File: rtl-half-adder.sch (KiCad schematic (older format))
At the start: 50 parts, among them Q1 Q_NPN_EBC, Q10 Q_NPN_EBC, Q11 Q_NPN_EBC, Q12 Q_NPN_EBC, Q13 Q_NPN_EBC, Q14 Q_NPN_EBC, Q15 Q_NPN_EBC, Q2 Q_NPN_EBC, Q3 Q_NPN_EBC, Q4 Q_NPN_EBC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

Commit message: add sheet annotations
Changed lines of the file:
@@
 encoding utf-8
 Sheet 1 2
-Title ""
-Date ""
-Rev ""
+Title "RTL Half Adder"
+Date "2019-06-12"
+Rev "v1"
 Comp ""
-Comment1 ""
-Comment2 ""
-Comment3 ""
-Comment4 ""
+Comment1 "creativecommons.org/licenses/by-nc-sa/4.0/"
+Comment2 "CC BY-NC-SA"
+Comment3 "github.com/tyehle/rtl-half-adder"
+Comment4 "Author: Tobin Yehle"
 $EndDescr
 Wire Wire Line
@@
 NoConn ~ 3450 1400
 NoConn ~ 3450 1950
+$Comp
+L Graphic:Logo_Open_Hardware_Large #LOGO?
+U 1 1 5D03E126
+P 6350 7200
+AR Path="/5D016A93/5D03E126" Ref="#LOGO?"  Part="1"
+AR Path="/5D03E126" Ref="#LOGO?"  Part="1"
+F 0 "#LOGO?" H 6350 7700 50  0001 C CNN
+F 1 "Logo_Open_Hardware_Large" H 6350 6800 50  0001 C CNN
+F 2 "" H 6350 7200 50  0001 C CNN
+F 3 "~" H 6350 7200 50  0001 C CNN
+	1    6350 7200
+	1    0    0    -1
+$EndComp
 $EndSCHEMATC

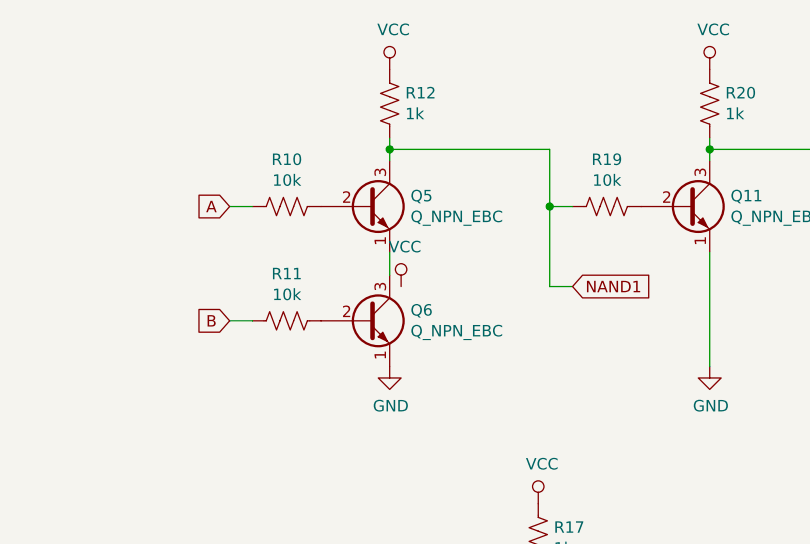
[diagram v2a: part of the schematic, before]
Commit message: more part links and BOM
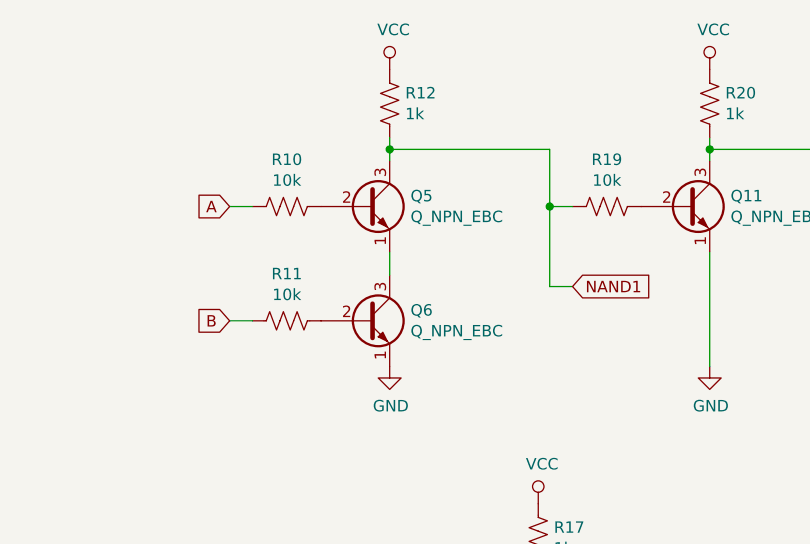
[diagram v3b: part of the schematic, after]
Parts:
- Q1, Q10, Q11, Q12, Q13, Q14, Q15, Q2, Q3, Q4, Q5, Q6, Q7, Q8, Q9: Link https://www.mouser.com/ProductDetail/PN2222A-T -> https://www.mouser.com/ProductDetail/2N3904BU
- R1, R10, R11, R13, R14, R15, R16, R19, R21, R22, R24, R25, R3, R5, R6, R7, R8: Link (none) -> https://www.mouser.com/ProductDetail/CFR-25JT-52-10K
- R12, R17, R18, R20, R23, R9: Link (none) -> https://www.mouser.com/ProductDetail/CFR-25JT-52-1K

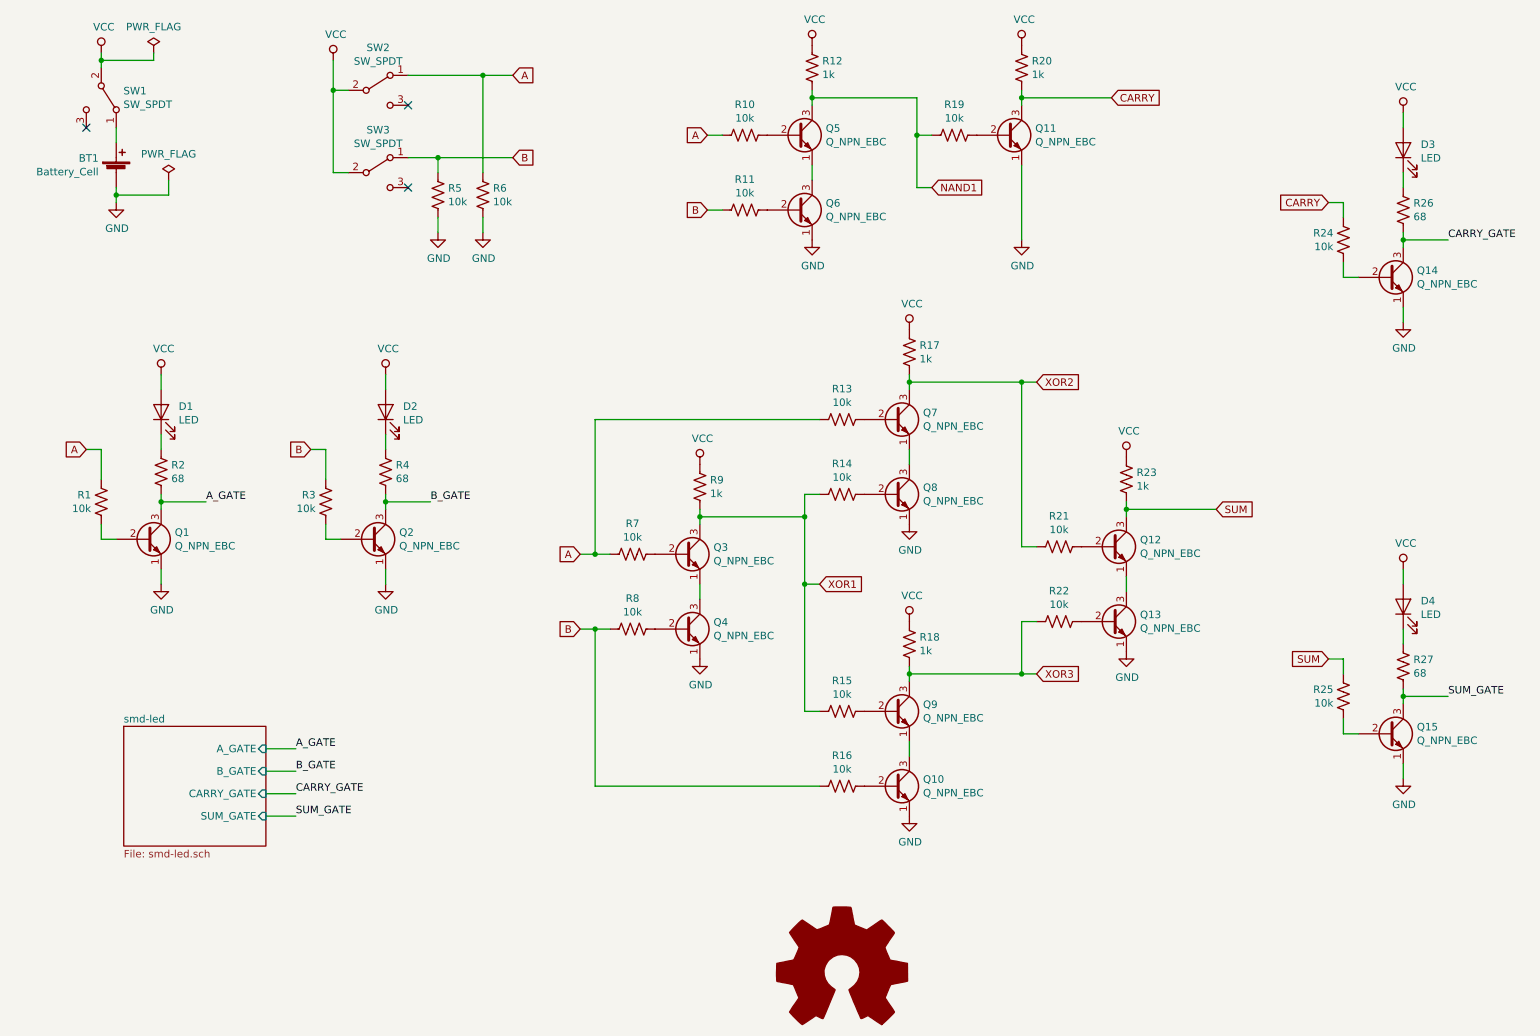
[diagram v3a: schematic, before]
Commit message: add io led specs
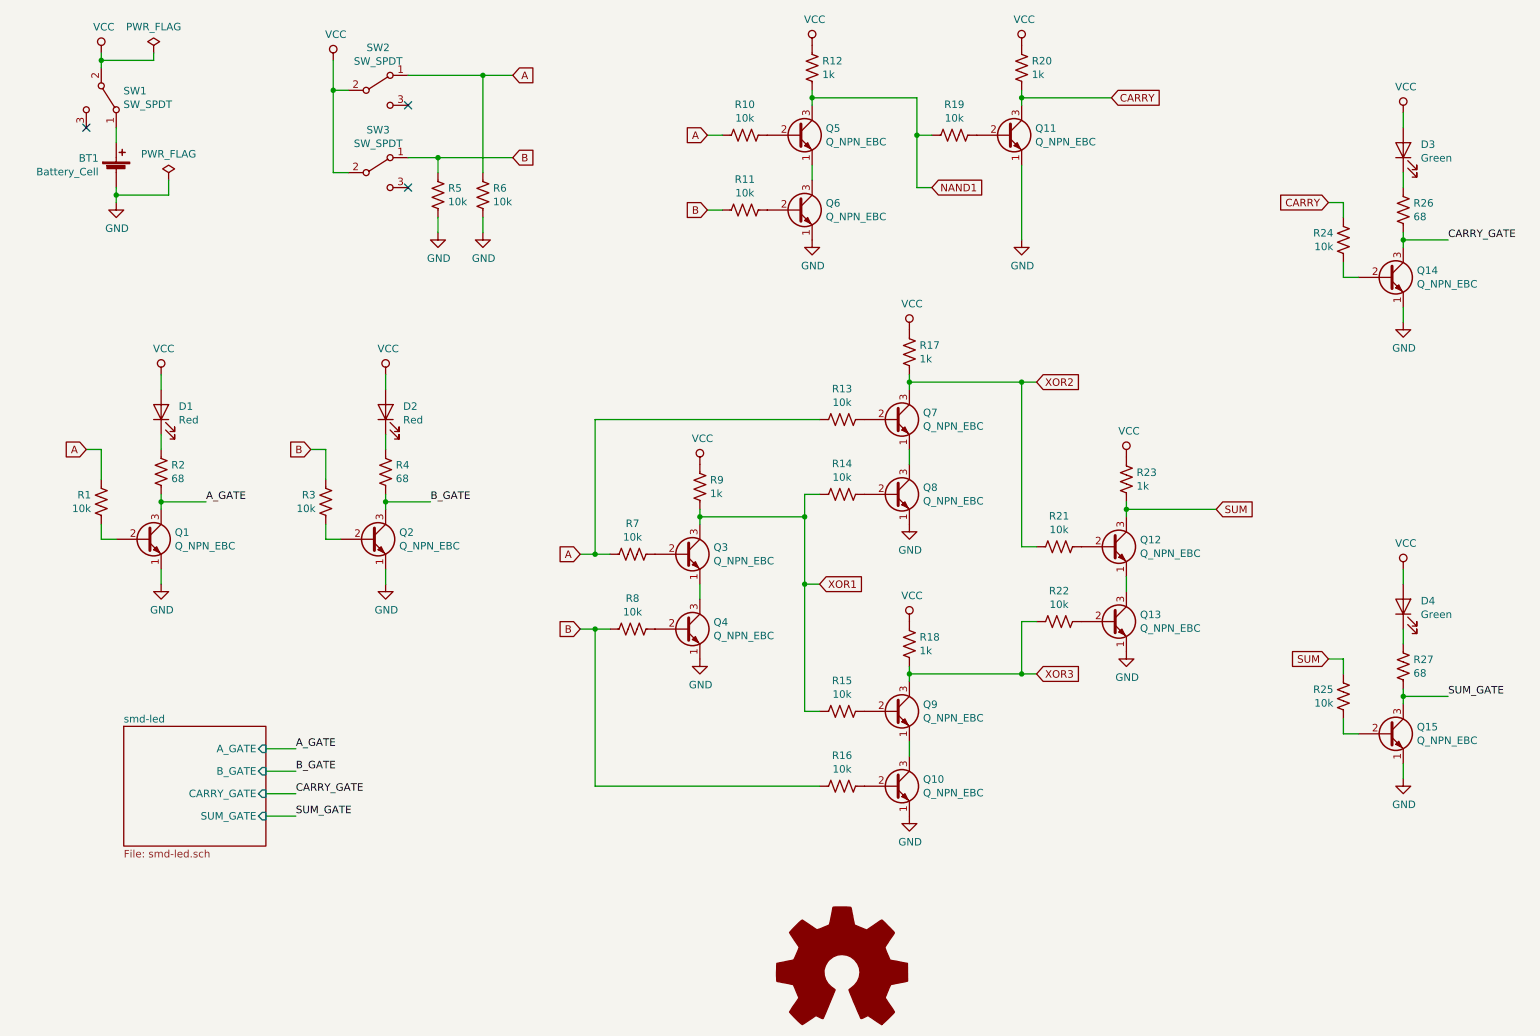
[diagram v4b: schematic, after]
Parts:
- D1, D2: value LED -> Red; Link (none) -> https://www.mouser.com/ProductDetail/LTL-4223
- D3, D4: value LED -> Green; Link (none) -> https://www.mouser.com/ProductDetail/LTL-4233
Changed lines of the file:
@@
 P 10100 1700
 F 0 "D3" V 10138 1583 50  0000 R CNN
-F 1 "LED" V 10047 1583 50  0000 R CNN
+F 1 "Green" V 10047 1583 50  0000 R CNN
 F 2 "LED_THT:LED_D5.0mm" H 10100 1700 50  0001 C CNN
-F 3 "~" H 10100 1700 50  0001 C CNN
+F 3 "https://optoelectronics.liteon.com/upload/download/DS-20-92-1097/4233DG.pdf" H 10100 1700 50  0001 C CNN
+F 4 "https://www.mouser.com/ProductDetail/LTL-4233" H 0   0   50  0001 C CNN "Link"
 	1    10100 1700
 	0    -1   -1   0
@@
 P 10100 4750
 F 0 "D4" V 10138 4633 50  0000 R CNN
-F 1 "LED" V 10047 4633 50  0000 R CNN
+F 1 "Green" V 10047 4633 50  0000 R CNN
 F 2 "LED_THT:LED_D5.0mm" H 10100 4750 50  0001 C CNN
-F 3 "~" H 10100 4750 50  0001 C CNN
+F 3 "https://optoelectronics.liteon.com/upload/download/DS-20-92-1097/4233DG.pdf" H 10100 4750 50  0001 C CNN
+F 4 "https://www.mouser.com/ProductDetail/LTL-4233" H 0   0   50  0001 C CNN "Link"
 	1    10100 4750
 	0    -1   -1   0
@@
 P 1800 3450
 F 0 "D1" V 1838 3333 50  0000 R CNN
-F 1 "LED" V 1747 3333 50  0000 R CNN
+F 1 "Red" V 1747 3333 50  0000 R CNN
 F 2 "LED_THT:LED_D5.0mm" H 1800 3450 50  0001 C CNN
-F 3 "~" H 1800 3450 50  0001 C CNN
+F 3 "https://optoelectronics.liteon.com/upload/download/DS20-2003-313/LTL-4223-032A.pdf" H 1800 3450 50  0001 C CNN
+F 4 "https://www.mouser.com/ProductDetail/LTL-4223" H 0   0   50  0001 C CNN "Link"
 	1    1800 3450
 	0    -1   -1   0
@@
 P 3300 3450
 F 0 "D2" V 3338 3333 50  0000 R CNN
-F 1 "LED" V 3247 3333 50  0000 R CNN
+F 1 "Red" V 3247 3333 50  0000 R CNN
 F 2 "LED_THT:LED_D5.0mm" H 3300 3450 50  0001 C CNN
-F 3 "~" H 3300 3450 50  0001 C CNN
+F 3 "https://optoelectronics.liteon.com/upload/download/DS20-2003-313/LTL-4223-032A.pdf" H 3300 3450 50  0001 C CNN
+F 4 "https://www.mouser.com/ProductDetail/LTL-4223" H 0   0   50  0001 C CNN "Link"
 	1    3300 3450
 	0    -1   -1   0

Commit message: finish bom
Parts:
- R2, R26, R27, R4: value 68 -> 510; Link (none) -> https://www.mouser.com/ProductDetail/CFR-25JR-52-510R
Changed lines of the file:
@@
 P 10100 2100
 F 0 "R26" H 10168 2146 50  0000 L CNN
-F 1 "68" H 10168 2055 50  0000 L CNN
+F 1 "510" H 10168 2055 50  0000 L CNN
 F 2 "Resistor_THT:R_Axial_DIN0207_L6.3mm_D2.5mm_P7.62mm_Horizontal" V 10140 2090 50  0001 C CNN
-F 3 "~" H 10100 2100 50  0001 C CNN
-F 4 "" H 0   0   50  0001 C CNN "Link"
+F 3 "http://www.yageo.com/NewPortal/yageodocoutput?fileName=/pdf/throughhole/Yageo_LR_CFR_2013.pdf" H 10100 2100 50  0001 C CNN
+F 4 "https://www.mouser.com/ProductDetail/CFR-25JR-52-510R" H 0   0   50  0001 C CNN "Link"
 	1    10100 2100
 	1    0    0    -1
@@
 P 10100 5150
 F 0 "R27" H 10168 5196 50  0000 L CNN
-F 1 "68" H 10168 5105 50  0000 L CNN
+F 1 "510" H 10168 5105 50  0000 L CNN
 F 2 "Resistor_THT:R_Axial_DIN0207_L6.3mm_D2.5mm_P7.62mm_Horizontal" V 10140 5140 50  0001 C CNN
-F 3 "~" H 10100 5150 50  0001 C CNN
-F 4 "" H 0   0   50  0001 C CNN "Link"
+F 3 "http://www.yageo.com/NewPortal/yageodocoutput?fileName=/pdf/throughhole/Yageo_LR_CFR_2013.pdf" H 10100 5150 50  0001 C CNN
+F 4 "https://www.mouser.com/ProductDetail/CFR-25JR-52-510R" H 0   0   50  0001 C CNN "Link"
 	1    10100 5150
 	1    0    0    -1
@@
 P 1800 3850
 F 0 "R2" H 1868 3896 50  0000 L CNN
-F 1 "68" H 1868 3805 50  0000 L CNN
+F 1 "510" H 1868 3805 50  0000 L CNN
 F 2 "Resistor_THT:R_Axial_DIN0207_L6.3mm_D2.5mm_P7.62mm_Horizontal" V 1840 3840 50  0001 C CNN
-F 3 "~" H 1800 3850 50  0001 C CNN
-F 4 "" H 0   0   50  0001 C CNN "Link"
+F 3 "http://www.yageo.com/NewPortal/yageodocoutput?fileName=/pdf/throughhole/Yageo_LR_CFR_2013.pdf" H 1800 3850 50  0001 C CNN
+F 4 "https://www.mouser.com/ProductDetail/CFR-25JR-52-510R" H 0   0   50  0001 C CNN "Link"
 	1    1800 3850
 	1    0    0    -1
@@
 P 3300 3850
 F 0 "R4" H 3368 3896 50  0000 L CNN
-F 1 "68" H 3368 3805 50  0000 L CNN
+F 1 "510" H 3368 3805 50  0000 L CNN
 F 2 "Resistor_THT:R_Axial_DIN0207_L6.3mm_D2.5mm_P7.62mm_Horizontal" V 3340 3840 50  0001 C CNN
-F 3 "~" H 3300 3850 50  0001 C CNN
-F 4 "" H 0   0   50  0001 C CNN "Link"
+F 3 "http://www.yageo.com/NewPortal/yageodocoutput?fileName=/pdf/throughhole/Yageo_LR_CFR_2013.pdf" H 3300 3850 50  0001 C CNN
+F 4 "https://www.mouser.com/ProductDetail/CFR-25JR-52-510R" H 0   0   50  0001 C CNN "Link"
 	1    3300 3850
 	1    0    0    -1
